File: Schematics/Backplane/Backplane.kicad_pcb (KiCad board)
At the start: 2 copper layers, 69.5 x 119 mm, 23 parts, among them J1 Edge Connector (SLOT 1), J2 Edge Connector (SLOT 2), J3 Edge Connector (SLOT 3), J4 Edge Connector (SLOT 4), J5 Edge Connector (SLOT 5), J6 Conn_01x06_Socket

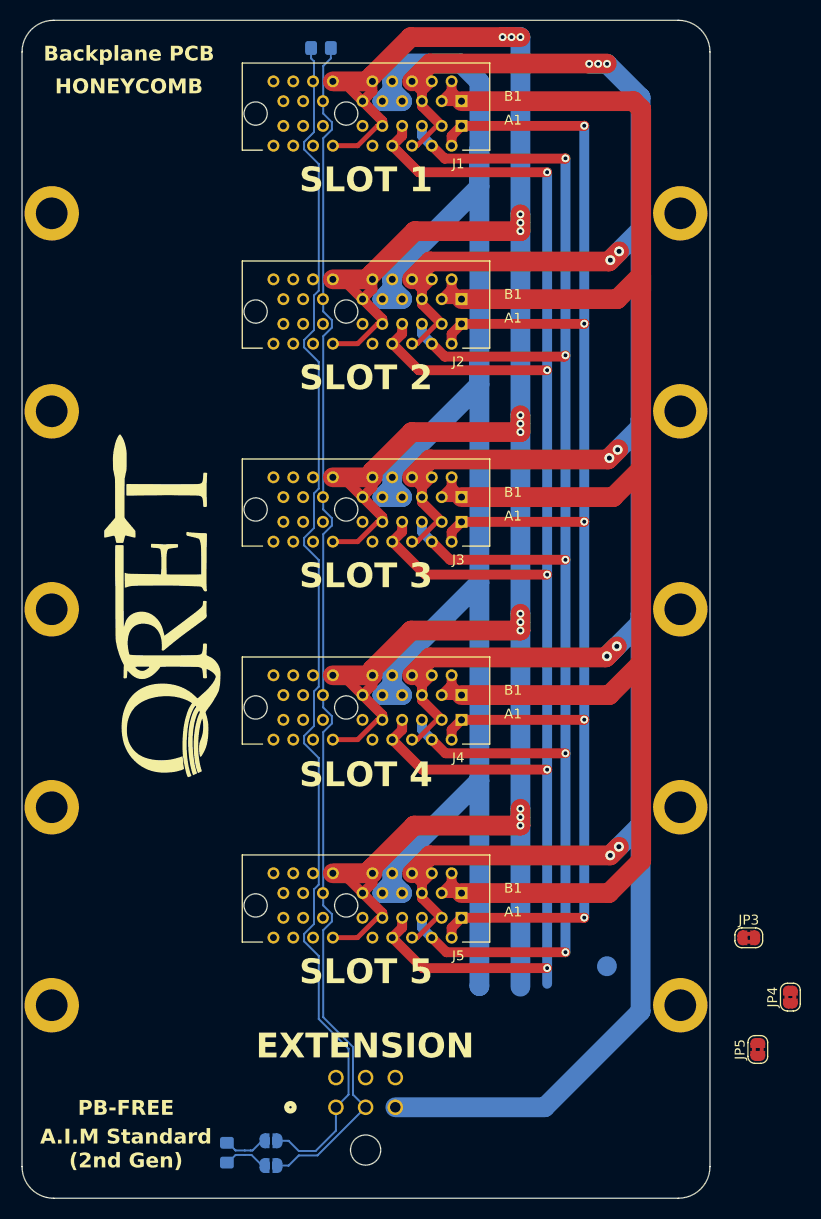
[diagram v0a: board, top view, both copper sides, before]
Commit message: updated backplane length to fit in stack design  - need to route traces to extension connector
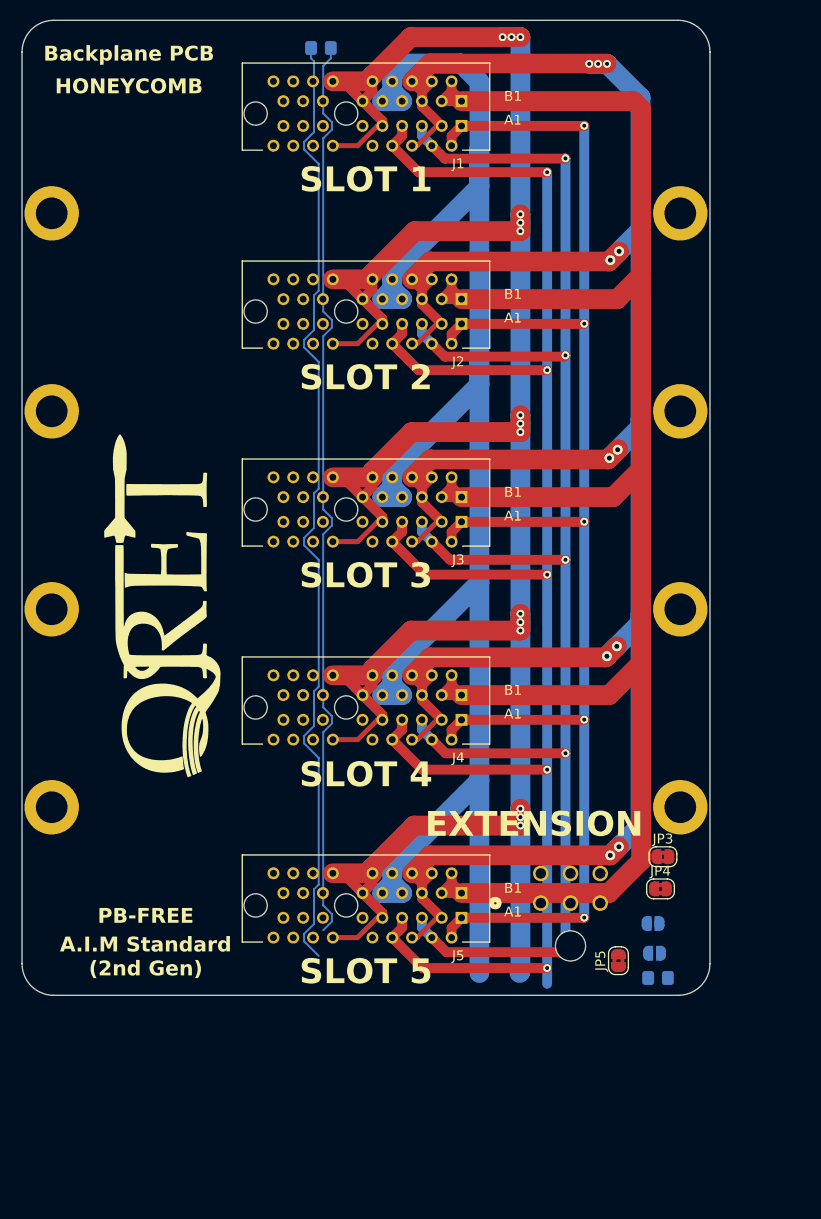
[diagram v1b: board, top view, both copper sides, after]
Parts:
- removed H10, H9: MountingHole, MountingHole:MountingHole_3.2mm_M3_ISO14580_Pad
- moved R2 47.0 mm to (64.2, 96.8), turned to 0 degrees
- moved JP1 45.7 mm to (63.8, 91.2)
- moved JP2 43.1 mm to (63.9, 94.2)
- moved J6 29.2 mm to (52.4, 89.2)
- moved JP4 17.1 mm to (64.5, 87.8), turned to 0 degrees
- moved JP5 16.7 mm to (60.2, 95.0)
- moved JP3 11.9 mm to (64.8, 84.5)
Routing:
- net GND1: track 320.6 -> 273.0 mm
- net CAN_N: track 124.1 -> 93.1 mm
- net CAN_P: track 124.4 -> 97.8 mm
- net /TERM_N: track 4.57 -> 0.00 mm
- net /TERM_P: track 4.52 -> 0.00 mm
- net GND2: track 287.2 -> 285.9 mm
- net BATT_B: track 191.8 -> 190.5 mm
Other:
- board size 69.5 x 119 mm -> 69.5 x 98.5 mm

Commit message: Backplane Trace
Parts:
- JP3, JP4, JP5: moved to B.Cu
- moved JP5 65.3 mm to (66.0, 30.0), turned to -90 degrees
- moved JP3 35.7 mm to (66.0, 48.9), turned to -90 degrees
- moved JP4 19.7 mm to (66.0, 68.2), turned to 90 degrees
- moved JP1 5.54 mm to (65.0, 85.8), turned to -90 degrees
- moved JP2 4.24 mm to (65.0, 90.2), turned to -90 degrees
- moved R2 1.90 mm to (65.0, 95.0)
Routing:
- net 24V_A: track 0.00 -> 234.1 mm
- net GND2: track 285.9 -> 167.9 mm, vias 15 -> 0
- net GND1: track 273.0 -> 357.1 mm, vias 11 -> 4
- net CAN_N: track 93.1 -> 142.9 mm
- net CAN_P: track 97.8 -> 139.4 mm
- net BATT_B: track 190.5 -> 218.7 mm, vias 0 -> 5
- net BATT_A: track 202.6 -> 178.3 mm, vias 0 -> 4
- net 3.3V_B: track 178.4 -> 198.6 mm, vias 5 -> 3
- net 5.0V_A: track 162.9 -> 153.1 mm, vias 5 -> 4
- net /TERM_N: track 0.00 -> 9.29 mm
- net 3.3V_A: track 154.1 -> 161.6 mm, vias 5 -> 4
- net /TERM_P: track 0.00 -> 4.61 mm

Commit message: start of my own backplane layout
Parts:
- JP3: value SolderJumper_2_Bridged -> 3.3V Bridge
- JP4: value SolderJumper_2_Bridged -> BATT Bridge
- JP5: value SolderJumper_2_Bridged -> GND Bridge
- moved JP4 68.4 mm to (43.3, 3.60)
- moved JP3 42.1 mm to (41.0, 15.0), turned to 180 degrees
- moved JP5 30.8 mm to (50.1, 3.54), turned to 180 degrees
- moved JP1 4.98 mm to (67.8, 90.0), turned to 0 degrees
- moved R2 2.28 mm to (65.9, 97.1)
- moved JP2 0.91 mm to (64.1, 90.0), turned to 180 degrees
- moved R1 0.20 mm to (30.2, 2.60)
- moved J6 0.09 mm to (52.5, 89.2)
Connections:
- J1 pad A15: 24V_A -> unconnected-(J1-Reserved-PadA15)
- J1 pad A17: 24V_A -> unconnected-(J1-Reserved-PadA17)
- J1 pad B15: GND1 -> unconnected-(J1-Reserved-PadB15)
- J1 pad B16: GND1 -> unconnected-(J1-Reserved-PadB16)
- J1 pad B17: GND1 -> unconnected-(J1-Reserved-PadB17)
- J1 pad B18: GND1 -> unconnected-(J1-Reserved-PadB18)
- J2 pad A15: 24V_A -> unconnected-(J2-Reserved-PadA15)
- J2 pad A17: 24V_A -> unconnected-(J2-Reserved-PadA17)
- J2 pad B15: GND1 -> unconnected-(J2-Reserved-PadB15)
- J2 pad B16: GND1 -> unconnected-(J2-Reserved-PadB16)
- J2 pad B17: GND1 -> unconnected-(J2-Reserved-PadB17)
- J2 pad B18: GND1 -> unconnected-(J2-Reserved-PadB18)
- J3 pad A15: 24V_A -> unconnected-(J3-Reserved-PadA15)
- J3 pad A17: 24V_A -> unconnected-(J3-Reserved-PadA17)
- J3 pad B15: GND1 -> unconnected-(J3-Reserved-PadB15)
- J3 pad B16: GND1 -> unconnected-(J3-Reserved-PadB16)
- J3 pad B17: GND1 -> unconnected-(J3-Reserved-PadB17)
- J3 pad B18: GND1 -> unconnected-(J3-Reserved-PadB18)
- J4 pad A15: 24V_A -> unconnected-(J4-Reserved-PadA15)
- J4 pad A17: 24V_A -> unconnected-(J4-Reserved-PadA17)
- J4 pad B15: GND1 -> unconnected-(J4-Reserved-PadB15)
- J4 pad B16: GND1 -> unconnected-(J4-Reserved-PadB16)
- J4 pad B17: GND1 -> unconnected-(J4-Reserved-PadB17)
- J4 pad B18: GND1 -> unconnected-(J4-Reserved-PadB18)
- J5 pad A15: 24V_A -> unconnected-(J5-Reserved-PadA15)
- J5 pad A17: 24V_A -> unconnected-(J5-Reserved-PadA17)
- J5 pad B15: GND1 -> unconnected-(J5-Reserved-PadB15)
- J5 pad B16: GND1 -> unconnected-(J5-Reserved-PadB16)
- J5 pad B17: GND1 -> unconnected-(J5-Reserved-PadB17)
- J5 pad B18: GND1 -> unconnected-(J5-Reserved-PadB18)
- J6 pad 1: CAN_P -> GND1
- J6 pad 3: GND1 -> CAN_P
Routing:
- net GND1: track 357.1 -> 166.7 mm, vias 4 -> 2
- net 24V_A: track 234.1 -> 128.8 mm, vias 0 -> 1
- net GND2: track 167.9 -> 242.5 mm, vias 0 -> 10
- net 3.3V_B: track 198.6 -> 125.3 mm, vias 3 -> 1
- net BATT_A: track 178.3 -> 114.5 mm
- net 3.3V_A: track 161.6 -> 101.2 mm, vias 4 -> 1
- net BATT_B: track 218.7 -> 162.5 mm, vias 5 -> 0
- net 5.0V_A: track 153.1 -> 119.6 mm, vias 4 -> 1
- net CAN_P: track 139.4 -> 145.0 mm
- net /TERM_P: track 4.61 -> 8.36 mm
- net CAN_N: track 142.9 -> 145.4 mm
- net /TERM_N: track 9.29 -> 8.38 mm
